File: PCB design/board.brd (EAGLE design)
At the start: 53.3 x 78.2 mm, 25 parts

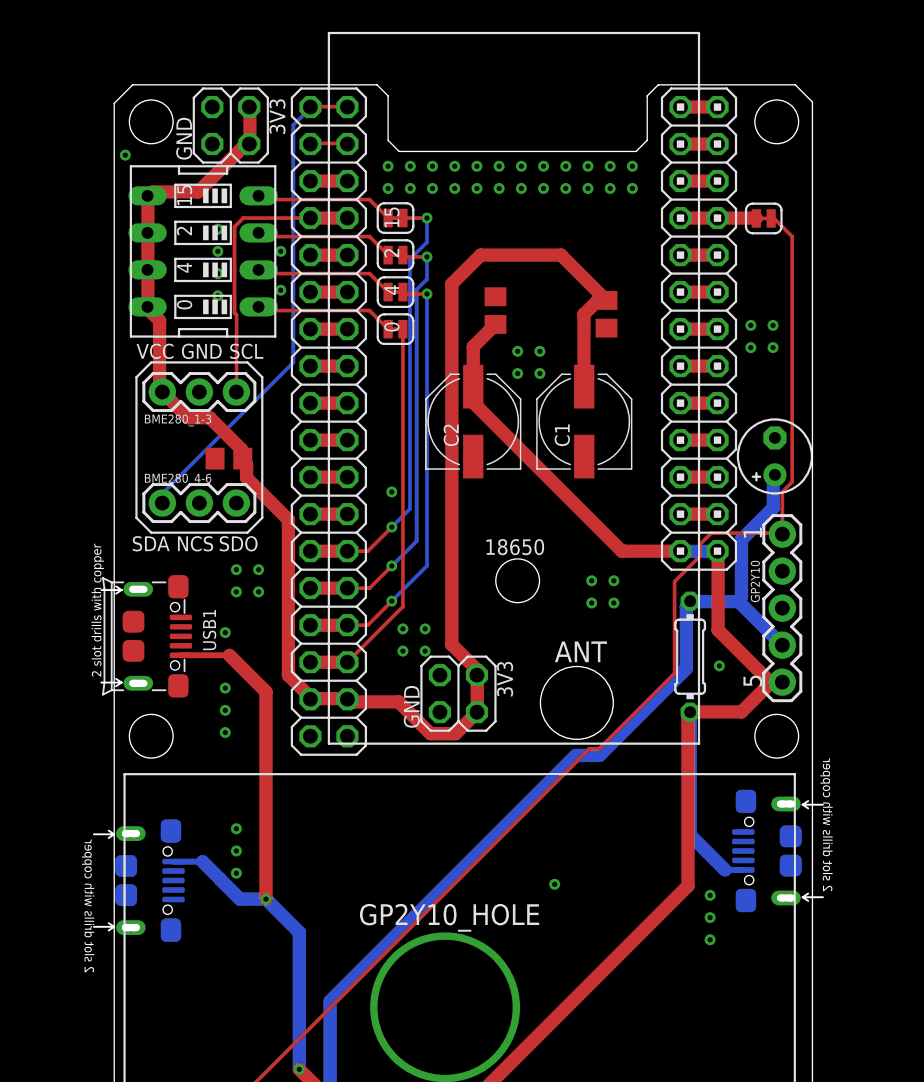
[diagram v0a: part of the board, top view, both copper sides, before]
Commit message: PCB issues update, pics cleanup
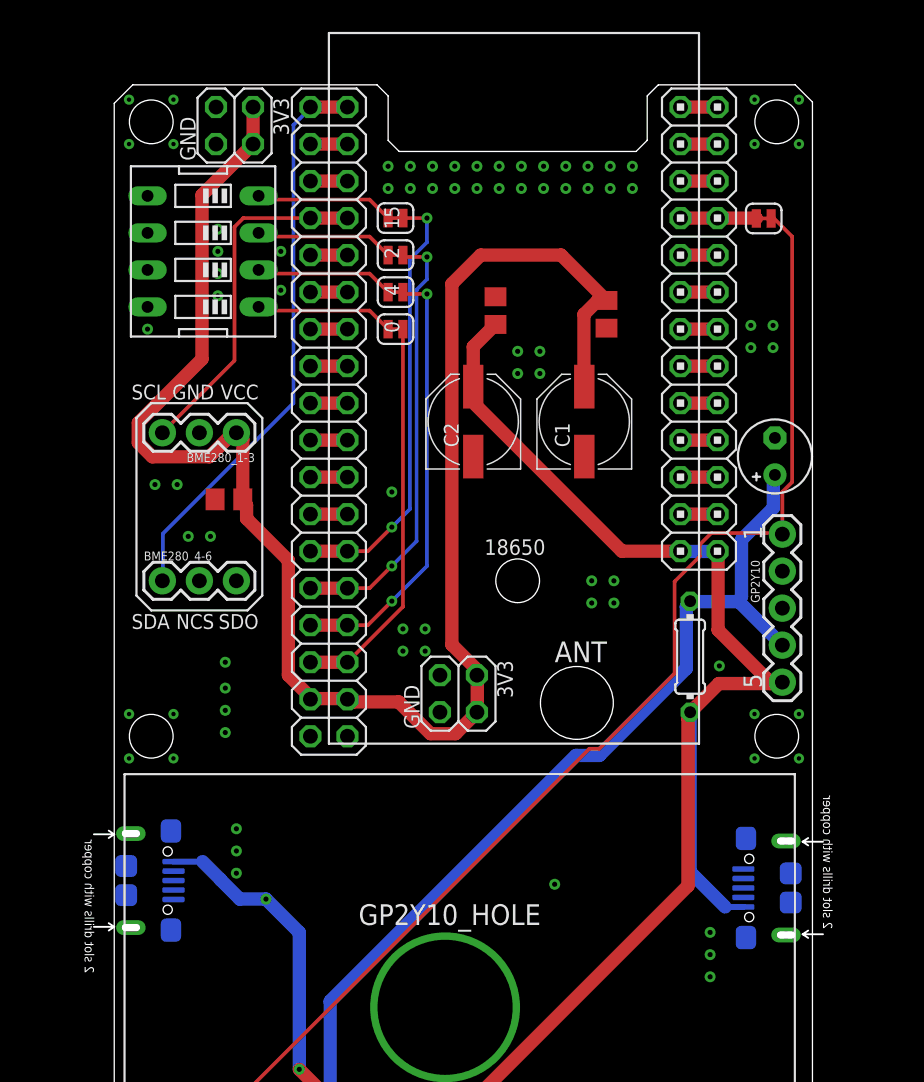
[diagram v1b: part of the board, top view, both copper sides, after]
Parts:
- removed USB1: ST-USB-001G, Seeed-Connector:MICRO-USB5+4P-SMD-0.65-B
- moved BME280_1-3 5.80 mm to (9.40, 26.2), turned to 180 degrees
- moved BME280_4-6 5.33 mm to (4.32, 16.0)
- moved C9 2.79 mm to (8.89, 21.6)
- moved USB2 2.54 mm to (43.9, -5.08)
- moved JP8 0.25 mm to (9.27, 47.2)
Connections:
- net 3.3V: no longer SW1.5, SW1.6, SW1.7, SW1.8
- net 5V: no longer USB1.5
- net GND: now also SW1.5, SW1.6, SW1.7, SW1.8; no longer USB1.1, USB1.S1, USB1.S2, USB1.S3, USB1.S4, USB1.S5, USB1.S6
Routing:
- net 5V: track 149.6 -> 131.1 mm
- net SDA: track 33.9 -> 39.2 mm
- net SCL: track 19.4 -> 24.2 mm
- net 3.3V: track 113.7 -> 117.3 mm
- net GND: vias 74 -> 90
